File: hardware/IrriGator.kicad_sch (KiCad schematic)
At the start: 44 parts, among them J1 L, J2 N, J3 230VAC, J4 36VDC, J5 Conn_01x04_Socket, J6 3V3, J7 Conn_01x04_Pin, J8 Conn_01x04_Pin, SW1 SW_Push, T1 24V 16VA, U1 ESP-01v090, U2 ATtiny45-20P, U3 DS3231-MINI-RTC, U4 ATtiny45-20P

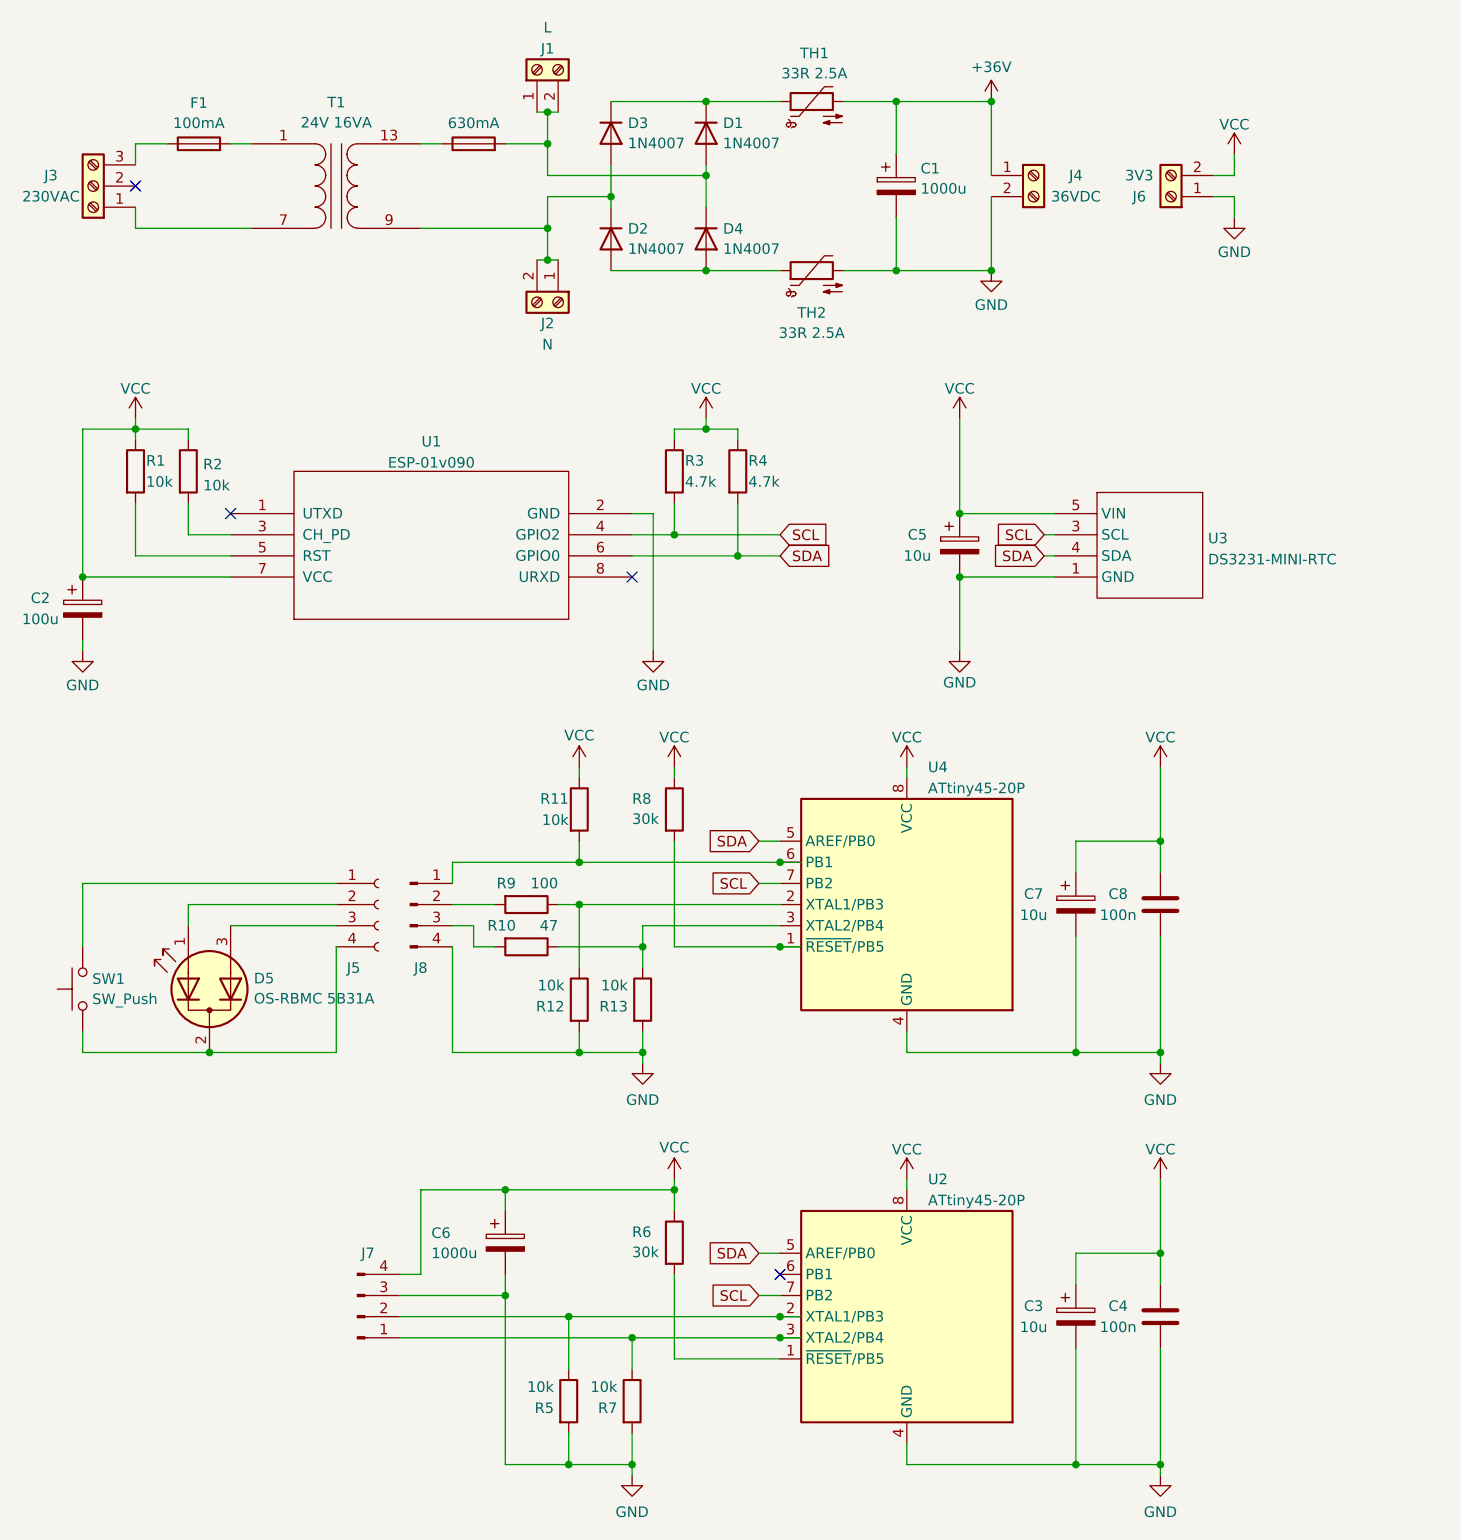
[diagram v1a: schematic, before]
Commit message: Updated PCB layout to better match the actual build
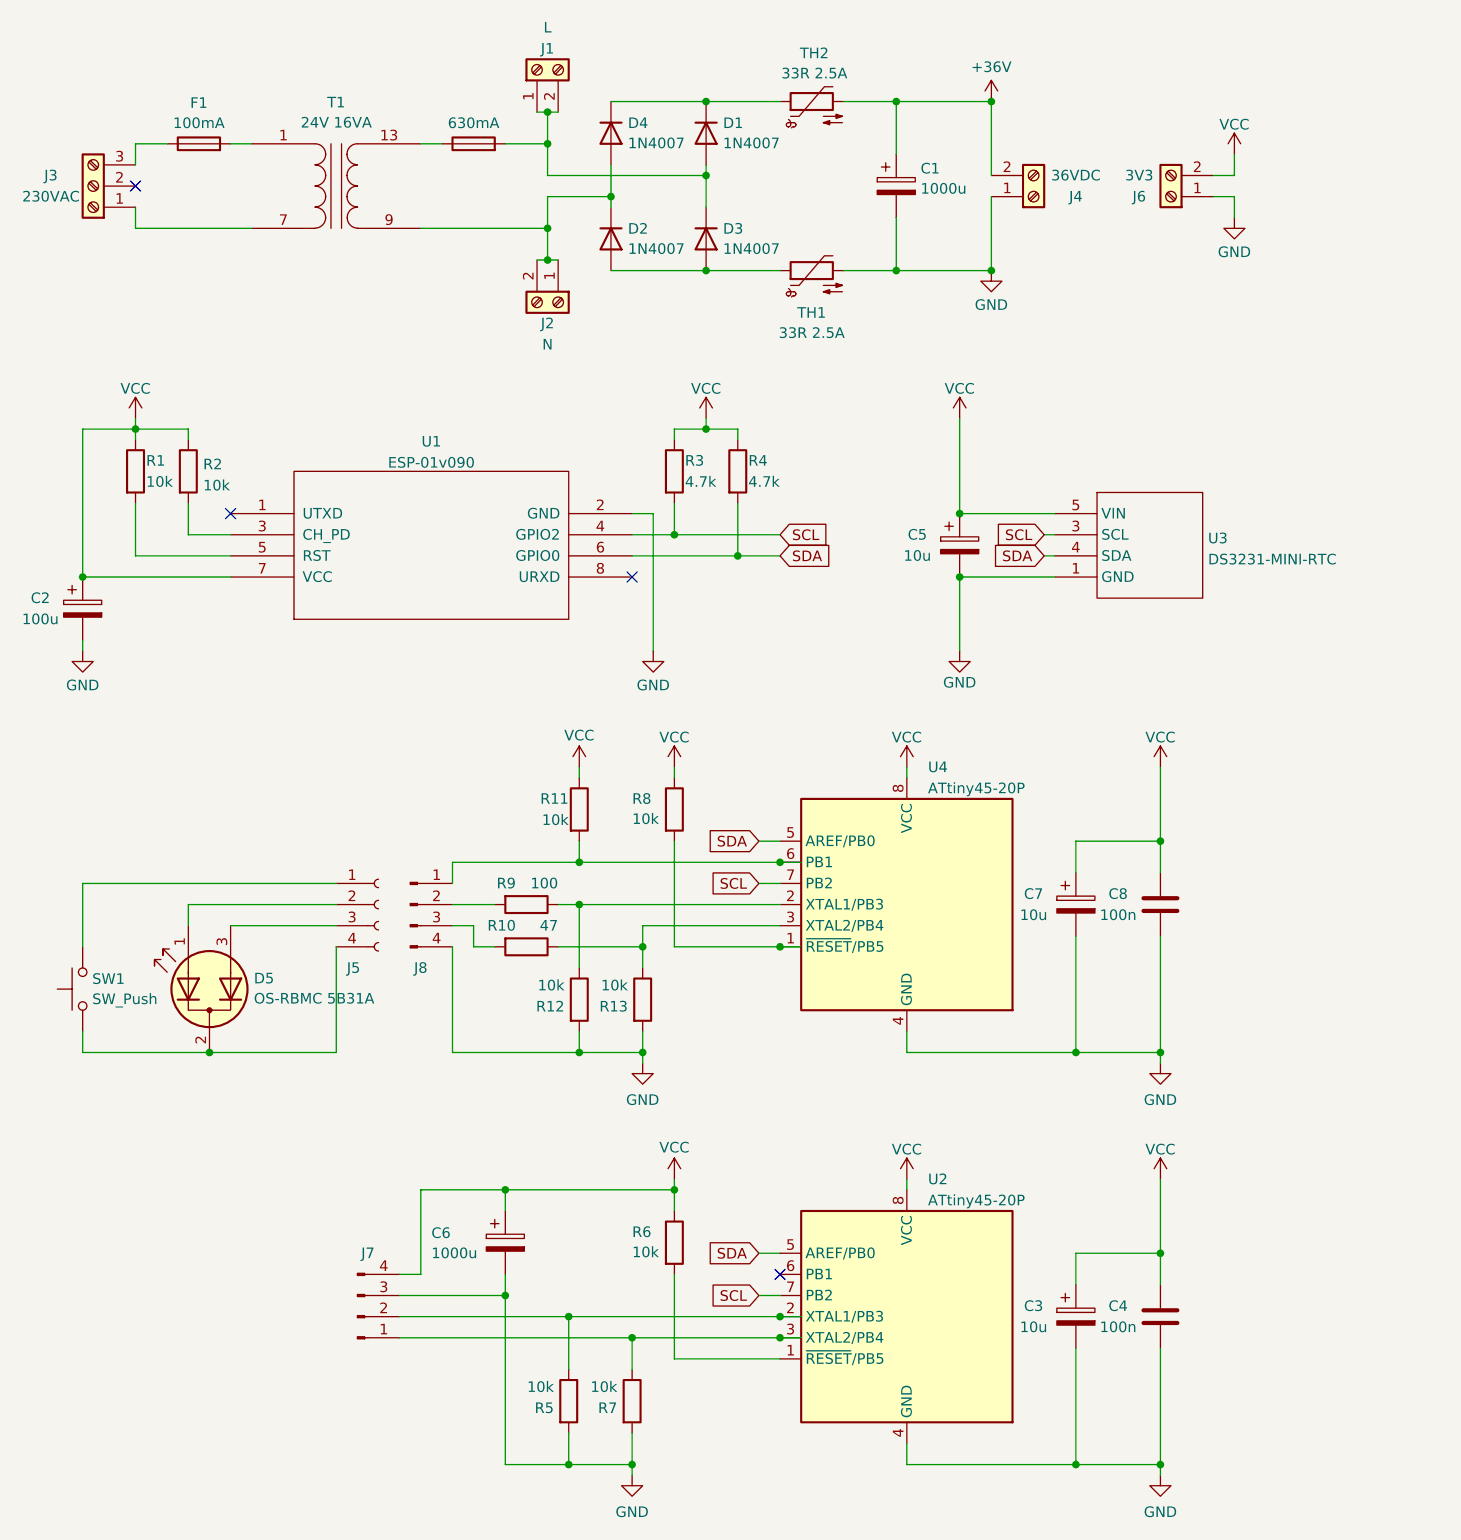
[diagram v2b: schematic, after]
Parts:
- R6, R8: value 30k -> 10k
- renumbered D4 to D3, D3 to D4, TH2 to TH1, TH1 to TH2
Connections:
- net +36V: now also J4.2 (Pin_2); no longer J4.1 (Pin_1)
- net GND: now also J4.1 (Pin_1); no longer J4.2 (Pin_2)
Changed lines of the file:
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@@
+    (stroke (width 0) (type default))
+  )
+  (wire (pts (xy 85.09 121.92) (xy 109.22 121.92))
+    (stroke (width 0) (type default))
+  )
+  (wire (pts (xy 81.28 44.45) (xy 80.01 44.45))
+    (stroke (width 0) (type default))
+  )
+  (wire (pts (xy 154.94 139.7) (xy 144.78 139.7))
+    (stroke (width 0) (type default))
+  )
+  (wire (pts (xy 93.98 74.93) (xy 93.98 91.44))
+    (stroke (width 0) (type default))
+  )
+  (wire (pts (xy 66.04 30.48) (xy 68.58 30.48))
+    (stroke (width 0) (type default))
+  )
+  (wire (pts (xy 85.09 105.41) (xy 85.09 106.68))
+    (stroke (width 0) (type default))
+  )
+  (wire (pts (xy 43.18 80.01) (xy 31.75 80.01))
+    (stroke (width 0) (type default))
+  )
+  (wire (pts (xy 76.2 30.48) (xy 81.28 30.48))
+    (stroke (width 0) (type default))
+  )
+  (wire (pts (xy 92.71 127) (xy 92.71 124.46))
+    (stroke (width 0) (type default))
+  )
+  (wire (pts (xy 109.22 173.99) (xy 91.44 173.99))
+    (stroke (width 0) (type default))
+  )
+  (wire (pts (xy 106.68 119.38) (xy 109.22 119.38))
+    (stroke (width 0) (type default))
+  )
+  (wire (pts (xy 100.33 25.4) (xy 109.22 25.4))
+    (stroke (width 0) (type default))
+  )
+  (wire (pts (xy 91.44 74.93) (xy 93.98 74.93))
+    (stroke (width 0) (type default))
+  )
+  (wire (pts (xy 85.09 116.84) (xy 109.22 116.84))
+    (stroke (width 0) (type default))
+  )
+  (wire (pts (xy 69.85 116.84) (xy 69.85 119.38))
+    (stroke (width 0) (type default))
+  )
+  (wire (pts (xy 144.78 163.83) (xy 154.94 163.83))
     (stroke (width 0) (type default))
   )
@@
     (stroke (width 0) (type default))
   )
-  (wire (pts (xy 85.09 121.92) (xy 109.22 121.92))
-    (stroke (width 0) (type default))
-  )
-  (wire (pts (xy 81.28 44.45) (xy 80.01 44.45))
-    (stroke (width 0) (type default))
-  )
-  (wire (pts (xy 154.94 139.7) (xy 144.78 139.7))
-    (stroke (width 0) (type default))
-  )
-  (wire (pts (xy 93.98 74.93) (xy 93.98 91.44))
-    (stroke (width 0) (type default))
-  )
-  (wire (pts (xy 66.04 30.48) (xy 68.58 30.48))
-    (stroke (width 0) (type default))
-  )
-  (wire (pts (xy 85.09 105.41) (xy 85.09 106.68))
-    (stroke (width 0) (type default))
-  )
-  (wire (pts (xy 43.18 80.01) (xy 31.75 80.01))
-    (stroke (width 0) (type default))
-  )
-  (wire (pts (xy 76.2 30.48) (xy 81.28 30.48))
-    (stroke (width 0) (type default))
-  )
-  (wire (pts (xy 92.71 127) (xy 92.71 124.46))
-    (stroke (width 0) (type default))
-  )
-  (wire (pts (xy 109.22 173.99) (xy 91.44 173.99))
-    (stroke (width 0) (type default))
-  )
-  (wire (pts (xy 106.68 119.38) (xy 109.22 119.38))
-    (stroke (width 0) (type default))
-  )
-  (wire (pts (xy 100.33 25.4) (xy 109.22 25.4))
-    (stroke (width 0) (type default))
-  )
-  (wire (pts (xy 91.44 74.93) (xy 93.98 74.93))
-    (stroke (width 0) (type default))
-  )
-  (wire (pts (xy 85.09 116.84) (xy 109.22 116.84))
-    (stroke (width 0) (type default))
-  )
-  (wire (pts (xy 69.85 116.84) (xy 69.85 119.38))
-    (stroke (width 0) (type default))
-  )
-  (wire (pts (xy 144.78 163.83) (xy 154.94 163.83))
-    (stroke (width 0) (type default))
-  )
   (wire (pts (xy 25.4 91.44) (xy 25.4 90.17))
     (stroke (width 0) (type default))
@@
     (stroke (width 0) (type default))
   )
+  (wire (pts (xy 134.62 34.29) (xy 134.62 25.4))
+    (stroke (width 0) (type default))
+  )
   (wire (pts (xy 154.94 139.7) (xy 154.94 140.97))
     (stroke (width 0) (type default))
@@
   )
   (wire (pts (xy 144.78 114.3) (xy 144.78 118.11))
-    (stroke (width 0) (type default))
-  )
-  (wire (pts (xy 134.62 34.29) (xy 134.62 25.4))
     (stroke (width 0) (type default))
   )
@@
   (symbol (lib_id "Diode:1N4007") (at 100.33 41.91 270) (unit 1)
     (in_bom yes) (on_board yes) (dnp no) (fields_autoplaced)
-    (property "Reference" "D4" (at 102.362 40.6979 90)
+    (property "Reference" "D3" (at 102.362 40.6979 90)
       (effects (font (size 1.27 1.27)) (justify left))
     )
@@
       (project "IrriGator"
         (path "/57674e40-bea9-402e-a85f-370abfe2d124"
-          (reference "D4") (unit 1)
+          (reference "D3") (unit 1)
         )
       )
@@
     )
   )
-  (symbol (lib_id "Connector:Screw_Terminal_01x02") (at 139.7 34.29 0) (unit 1)
-    (in_bom yes) (on_board yes) (dnp no)
-    (property "Reference" "J4" (at 144.78 34.29 0)
-      (effects (font (size 1.27 1.27)))
-    )
-    (property "Value" "36VDC" (at 144.78 36.83 0)
-      (effects (font (size 1.27 1.27)))
-    )
-    (property "Footprint" "TerminalBlock_Phoenix:TerminalBlock_Phoenix_MKDS-1,5-2-5.08_1x02_P5.08mm_Horizontal" (at 139.7 34.29 0)
-      (effects (font (size 1.27 1.27)) hide)
-    )
-    (property "Datasheet" "~" (at 139.7 34.29 0)
+  (symbol (lib_id "Connector:Screw_Terminal_01x02") (at 139.7 36.83 0) (mirror x) (unit 1)
+    (in_bom yes) (on_board yes) (dnp no)
+    (property "Reference" "J4" (at 144.78 36.83 0)
+      (effects (font (size 1.27 1.27)))
+    )
+    (property "Value" "36VDC" (at 144.78 34.29 0)
+      (effects (font (size 1.27 1.27)))
+    )
+    (property "Footprint" "TerminalBlock_Phoenix:TerminalBlock_Phoenix_MKDS-1,5-2-5.08_1x02_P5.08mm_Horizontal" (at 139.7 36.83 0)
+      (effects (font (size 1.27 1.27)) hide)
+    )
+    (property "Datasheet" "~" (at 139.7 36.83 0)
       (effects (font (size 1.27 1.27)) hide)
     )
@@
   (symbol (lib_id "Diode:1N4007") (at 88.9 29.21 270) (unit 1)
     (in_bom yes) (on_board yes) (dnp no) (fields_autoplaced)
-    (property "Reference" "D3" (at 90.932 27.9979 90)
+    (property "Reference" "D4" (at 90.932 27.9979 90)
       (effects (font (size 1.27 1.27)) (justify left))
     )
@@
       (project "IrriGator"
         (path "/57674e40-bea9-402e-a85f-370abfe2d124"
-          (reference "D3") (unit 1)
+          (reference "D4") (unit 1)
         )
       )
@@
   (symbol (lib_id "Device:Thermistor_NTC") (at 113.03 45.72 90) (unit 1)
     (in_bom yes) (on_board yes) (dnp no)
-    (property "Reference" "TH2" (at 113.03 50.8 90)
+    (property "Reference" "TH1" (at 113.03 50.8 90)
       (effects (font (size 1.27 1.27)))
     )
@@
       (project "IrriGator"
         (path "/57674e40-bea9-402e-a85f-370abfe2d124"
-          (reference "TH2") (unit 1)
+          (reference "TH1") (unit 1)
         )
       )
@@
   (symbol (lib_id "Device:Thermistor_NTC") (at 113.03 25.4 90) (unit 1)
     (in_bom yes) (on_board yes) (dnp no) (fields_autoplaced)
-    (property "Reference" "TH1" (at 113.3475 19.6047 90)
+    (property "Reference" "TH2" (at 113.3475 19.6047 90)
       (effects (font (size 1.27 1.27)))
     )
@@
       (project "IrriGator"
         (path "/57674e40-bea9-402e-a85f-370abfe2d124"
-          (reference "TH1") (unit 1)
+          (reference "TH2") (unit 1)
         )
       )
@@
       (effects (font (size 1.27 1.27)) (justify left))
     )
-    (property "Value" "30k" (at 91.44 111.6442 0)
+    (property "Value" "10k" (at 91.44 111.6442 0)
       (effects (font (size 1.27 1.27)) (justify left))
     )
@@
       (effects (font (size 1.27 1.27)) (justify left))
     )
-    (property "Value" "30k" (at 91.44 163.7142 0)
-      (effects (font (size 1.27 1.27)) (justify left))
-    )
+    (property "Value" "10k" (at 91.44 163.7142 0)
+      (effects (font (size 1.27 1.27)) (justify left))
+    )

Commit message: Added UART debug pins to the hardware
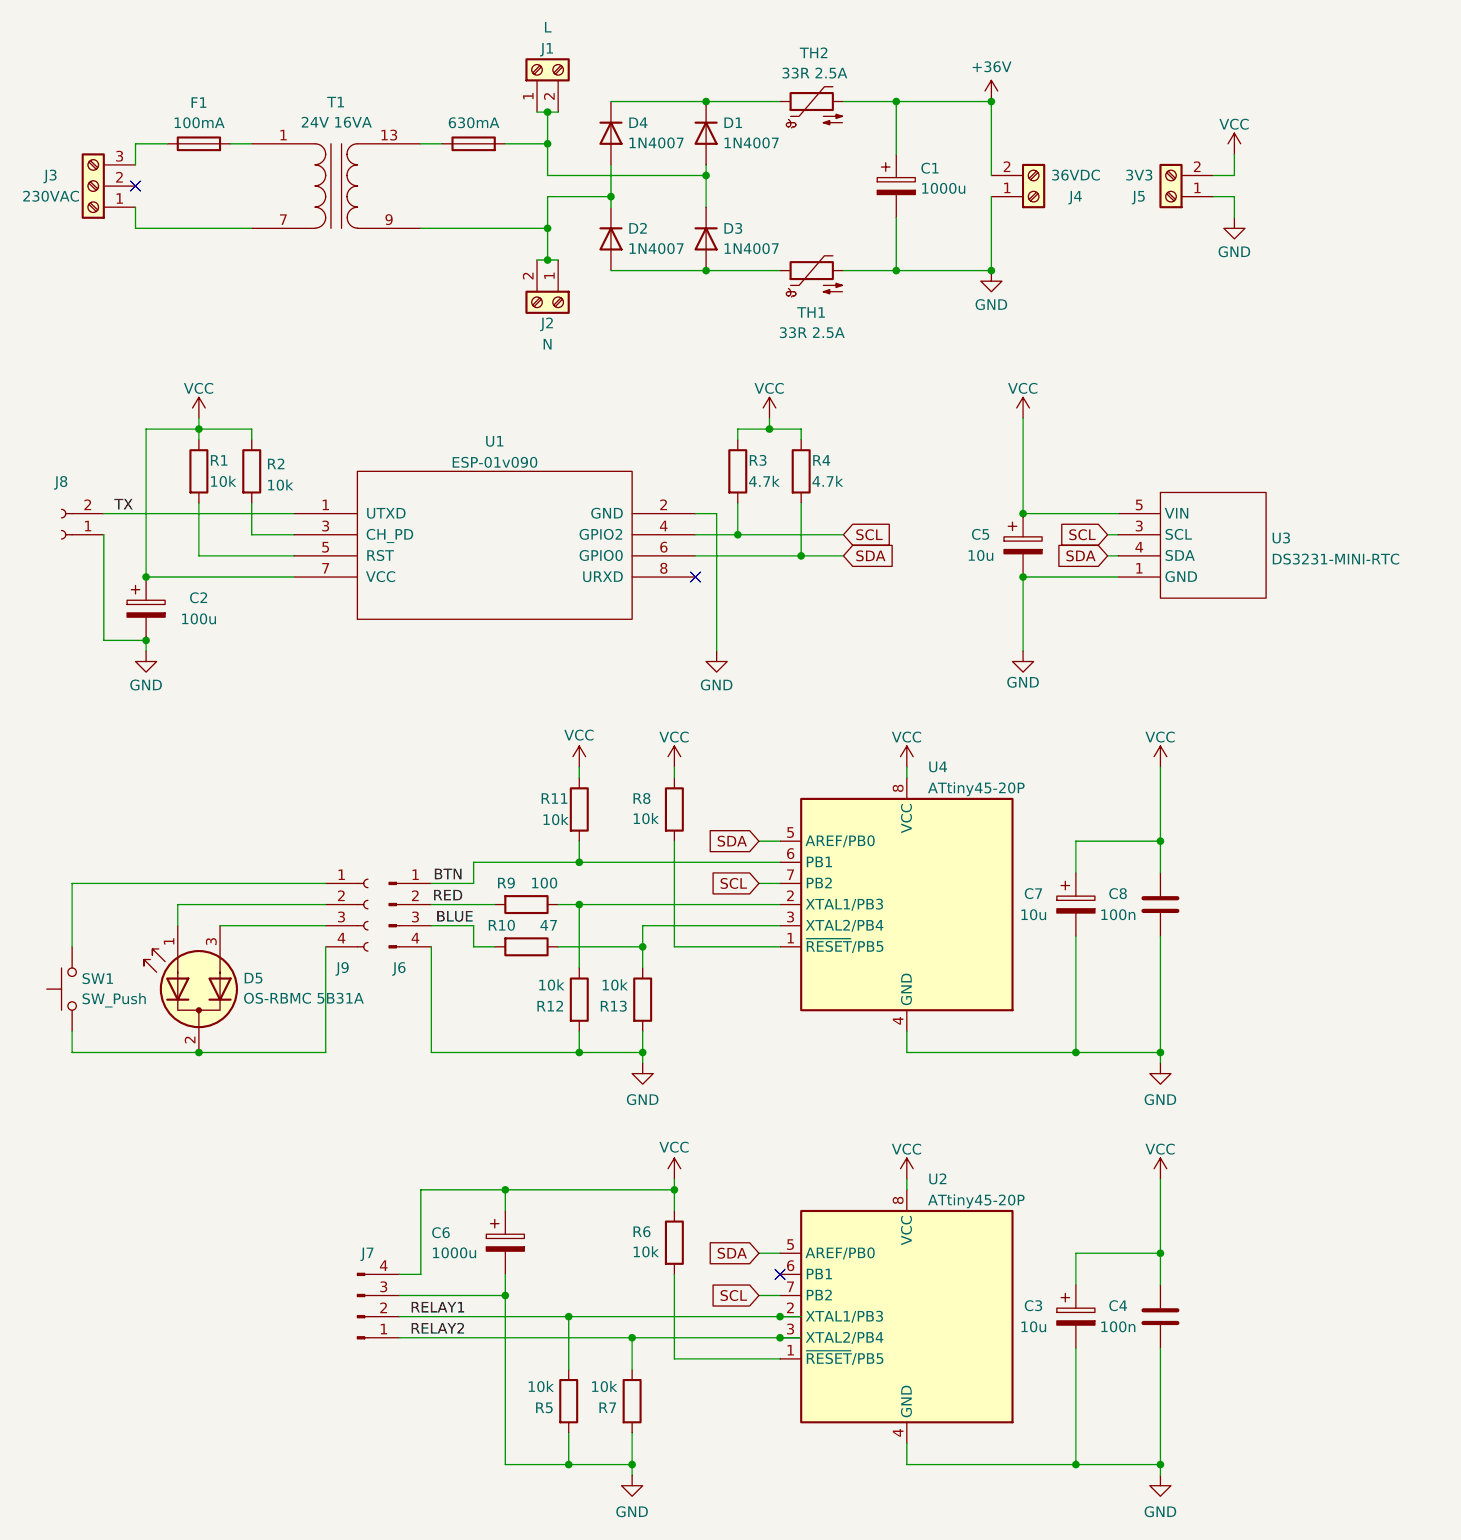
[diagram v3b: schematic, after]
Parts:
- added J8: Conn_01x02_Socket, Connector_PinSocket_2.54mm:PinSocket_1x02_P2.54mm_Vertical, symbol Connector:Conn_01x02_Socket
- renumbered J6 to J5, J8 to J6, J5 to J9
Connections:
- net GND: now also J8.1 (Pin_1)
- net RELAY1: now reaches J7.2 (Pin_2), R5.1, U2.2 (XTAL1/PB3)
- net RELAY2: now reaches J7.1 (Pin_1), R7.1, U2.3 (XTAL2/PB4)
- net BTN: now reaches J6.1 (Pin_1), R11.2, U4.6 (PB1)
- net RED: now reaches J6.2 (Pin_2), R9.2
- net BLUE: now reaches J6.3 (Pin_3), R10.2
- net TX: now reaches U1.1 (UTXD)
- net TX: now also J8.2 (Pin_2)
- no-connect marks 4 -> 3
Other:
- moved on the sheet: C2, C5, D5, J6, J9, R1, R2, R3, R4, SW1, U1, U3
